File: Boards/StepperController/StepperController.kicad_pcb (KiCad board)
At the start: 2 copper layers, 164 parts, among them IC1 ATMEGA645A-A, J1 I2C, J2 SPI_Extern, J3 ISP, J4 Reference, J5 Display, J7 Spindle, P1 Power, P10 CONN_Z, P2 Cover, P3 USB_B, P4 Relay2, P5 Relay1, P6 Emer_Off, P8 CONN_X, P9 CONN_Y, Q1 BC817-40, Q2 BC817-40, Q3 BC817-40, Q4 BC817-40, Q5 BC817-40, SW2 SW_1, SW3 SW_2, U1 LM2595S-5, U2 74LS11, U3 FT232RL, U5 TMC2660, U6 TMC2660, U7 TMC2660, U8 74HC00, X1 16MHz, Y1 20MHz

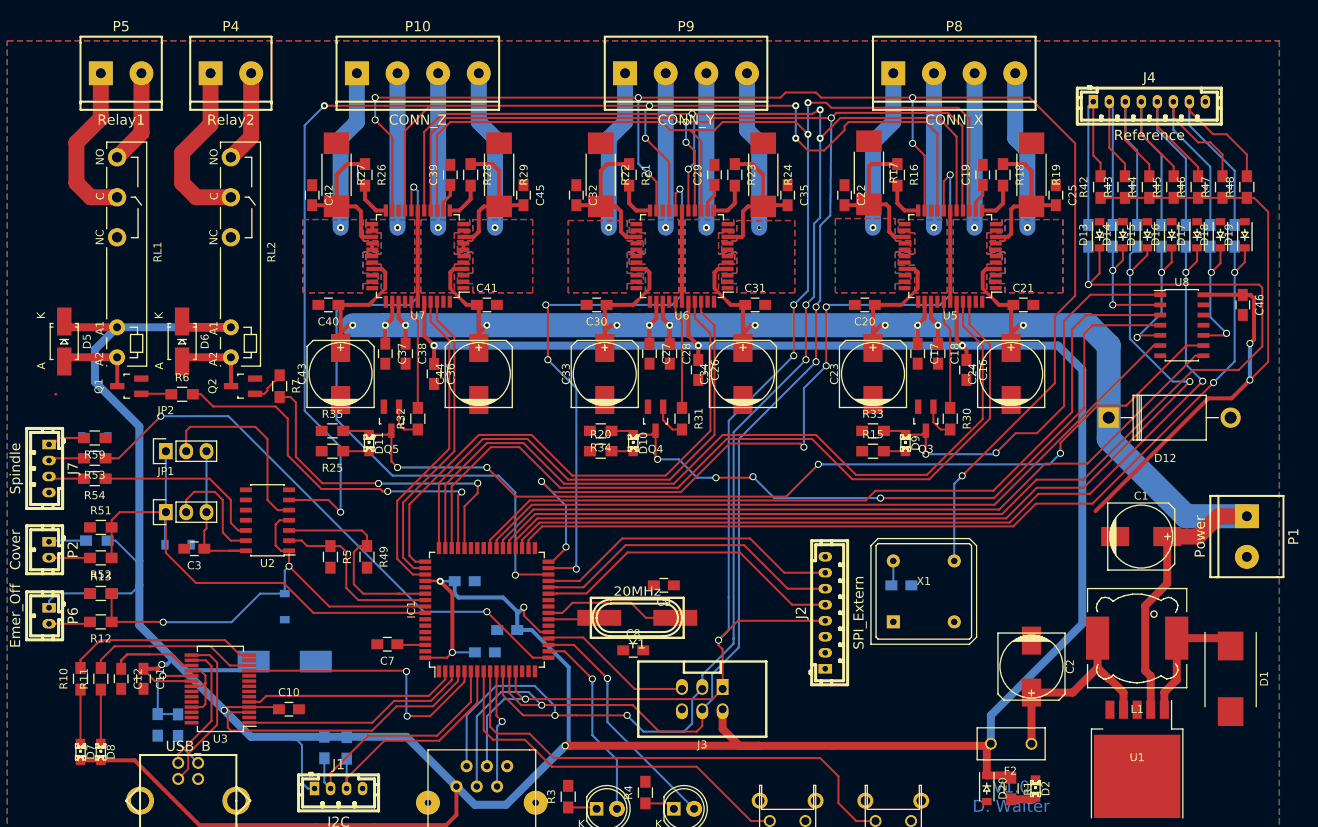
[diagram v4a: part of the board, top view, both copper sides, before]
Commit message: Layouting... Neuer Oszillator für TMC
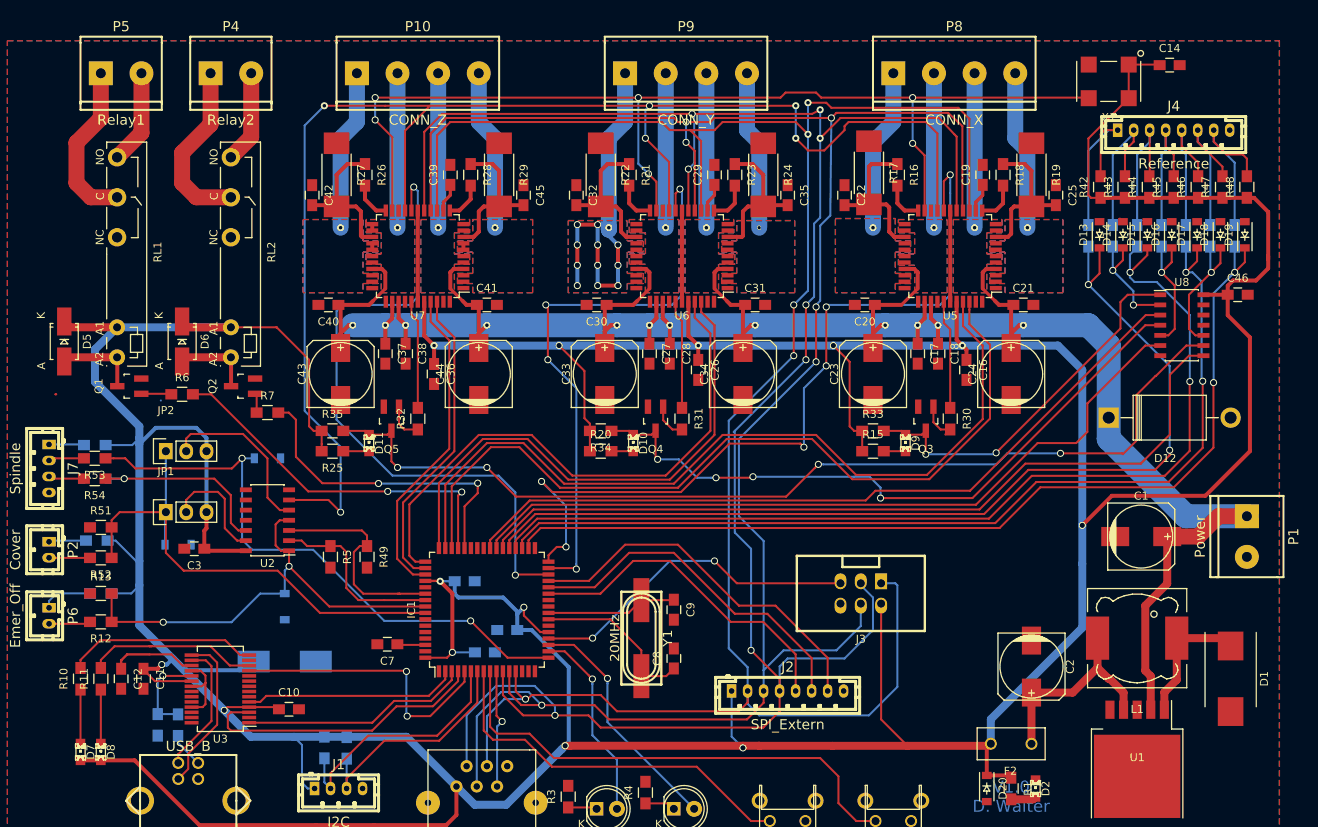
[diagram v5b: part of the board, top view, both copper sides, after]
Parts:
- C14: moved to F.Cu
- R59: moved to B.Cu
- X1: footprint Oscillators:OSC_DIP8 -> Oscillators_SMD:XO91
- moved C14 73.2 mm to (209.3, 56.9)
- moved X1 67.8 mm to (201.7, 58.9), turned to 180 degrees
- moved J3 23.8 mm to (170.7, 122.9)
- moved D22 21.8 mm to (96.5, 106.0), turned to 0 degrees
- moved J2 10.8 mm to (161.5, 135.1), turned to 0 degrees
- moved C8 5.18 mm to (147.3, 131.1), turned to 90 degrees
- moved J4 4.68 mm to (209.8, 65.0)
- moved R7 3.64 mm to (96.5, 100.3), turned to 0 degrees
- moved C9 3.29 mm to (147.3, 125.0), turned to 270 degrees
- moved Y1 2.59 mm to (143.3, 128.5), turned to 270 degrees
- moved C46 1.42 mm to (217.8, 85.6), turned to 0 degrees
- moved R59 0.89 mm to (74.9, 104.4)
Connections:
- J2 pad 2: /Controller/SCK -> /Controller/SDO
- J2 pad 4: /Controller/SDO -> /Controller/SCK
- X1 pad 1: (no net) -> +5V
- X1 pad 4: GND -> +5V
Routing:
- net +5V: track 625.9 -> 734.7 mm, vias 11 -> 13
- net /Driver/Driver_X/TMC_Clock: track 193.6 -> 134.5 mm, vias 7 -> 6
- net /Controller/SCK: track 235.0 -> 267.6 mm
- net /Controller/SDO: track 236.2 -> 265.0 mm, vias 6 -> 5
- net /Driver/Driver_Y/OB1_Y: track 20.1 -> 48.7 mm, vias 1 -> 12
- net Net-(IC1-Pad20): track 19.4 -> 41.8 mm, vias 0 -> 2
- net /Controller/SDI: track 231.2 -> 252.5 mm
- net /Controller/Ref_X1: track 144.3 -> 123.4 mm, vias 1 -> 2
- net Net-(C8-Pad1): track 6.42 -> 20.9 mm
- net Net-(J4-Pad6): track 30.1 -> 19.6 mm
- net Net-(J4-Pad5): track 28.3 -> 18.7 mm
- net Net-(J4-Pad7): track 31.0 -> 21.6 mm
- net Net-(J4-Pad4): track 28.2 -> 19.0 mm
- net Net-(J4-Pad3): track 27.4 -> 19.1 mm
- net Net-(IC1-Pad29): track 38.6 -> 46.8 mm
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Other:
- rule trace_min: 0.15 -> 0.254

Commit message: Layouting...
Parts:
- added G***: LOGO, Loewe:Loewe_Klein, F.Cu at (178.8, 139.2)
- added REF**: EuroBoard160mmX100mm_holes, Euro:EuroBoard160mmX100mm_holes, F.Cu at (64.0, 152.9)
- added REF**: Symbol_HighVoltage_Type2_CopperTop_VerySmall, Symbols:Symbol_HighVoltage_Type2_CopperTop_VerySmall, B.Cu at (84.8, 79.2)
- C11: moved to B.Cu
- moved C11 3.82 mm to (77.2, 133.9), turned to 180 degrees
- moved X1 2.80 mm to (204.5, 59.1)
- moved D2 2.74 mm to (189.9, 148.0), turned to 0 degrees
- moved J7 2.62 mm to (69.8, 104.8)
- moved D20 2.29 mm to (184.2, 147.3)
- moved C14 2.16 mm to (210.8, 58.4), turned to 90 degrees
- moved P2 1.42 mm to (69.8, 116.2)
- moved P6 1.42 mm to (69.8, 127.0)
- moved R1 1.33 mm to (189.9, 146.1), turned to 0 degrees
- moved C17 1.02 mm to (176.8, 93.0)
- moved C28 1.02 mm to (145.8, 93.0)
- moved C34 1.02 mm to (157.0, 95.5)
- moved P8 1.02 mm to (181.4, 57.9)
- moved C43 1.02 mm to (104.6, 95.5)
- moved C18 1.02 mm to (179.3, 93.0)
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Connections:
- net /Driver/Driver_Y/BRN_Y renamed /Driver/Driver_Y/BRB_Y
- R28 pad 2: /Driver/Driver_Z/BRB_Z -> /Driver/Driver_Z/SRA_Z
- U7 pad 12: /Driver/Driver_Z/BRB_Z -> /Driver/Driver_Z/SRA_Z
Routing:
- net GND: track 43.6 -> 207.2 mm, vias 0 -> 16
- net /Driver/Driver_Z/OB1_Z: track 20.9 -> 53.1 mm, vias 1 -> 12
- net /Driver/Driver_Y/OA1_Y: track 19.9 -> 51.1 mm, vias 1 -> 11
- net /Driver/Driver_X/OA1_X: track 19.9 -> 50.2 mm, vias 1 -> 12
- net /Driver/Driver_X/OB1_X: track 20.4 -> 49.9 mm, vias 1 -> 12
- net /Driver/Driver_Z/OA1_Z: track 20.9 -> 47.9 mm, vias 1 -> 11
- net /Driver/Sup_36V: track 309.7 -> 295.4 mm
- net +5V: track 734.7 -> 748.2 mm
- net /Driver/Driver_Y/OB2_Y: track 19.3 -> 27.0 mm, vias 1 -> 5
- net /Driver/Driver_X/TMC_Enable: track 183.0 -> 190.4 mm
- net /Driver/Driver_Y/OA2_Y: track 19.3 -> 26.6 mm, vias 1 -> 4
- net /Driver/Driver_Z/OB2_Z: track 20.1 -> 27.2 mm, vias 1 -> 4
- net /Driver/Driver_Z/OA2_Z: track 19.3 -> 26.4 mm, vias 1 -> 4
- net /Driver/Driver_X/OA2_X: track 19.3 -> 26.1 mm, vias 1 -> 4
- net /Driver/Driver_X/OB2_X: track 19.3 -> 26.0 mm, vias 1 -> 4
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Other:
- board outline added: 160 x 100 mm
- board text added: "Bot"
- board text added: "TMC226 StepperController"
- board text added: "Top"

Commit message: Minor layout changes
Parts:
- moved G*** 3.34 mm to (179.3, 135.9)
- moved D3 1.52 mm to (137.7, 148.3)
- moved D4 1.52 mm to (147.3, 148.3)
- moved SW2 0.38 mm to (161.5, 150.0)
- moved SW3 0.38 mm to (174.8, 150.0)
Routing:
- net Net-(D3-Pad2): track 24.4 -> 22.9 mm
- net Net-(D3-Pad1): track 3.63 -> 4.76 mm
- net Net-(D4-Pad2): track 29.9 -> 30.8 mm
- net Net-(P4-Pad1): track 18.6 -> 19.5 mm
- net Net-(P5-Pad1): track 18.5 -> 19.1 mm

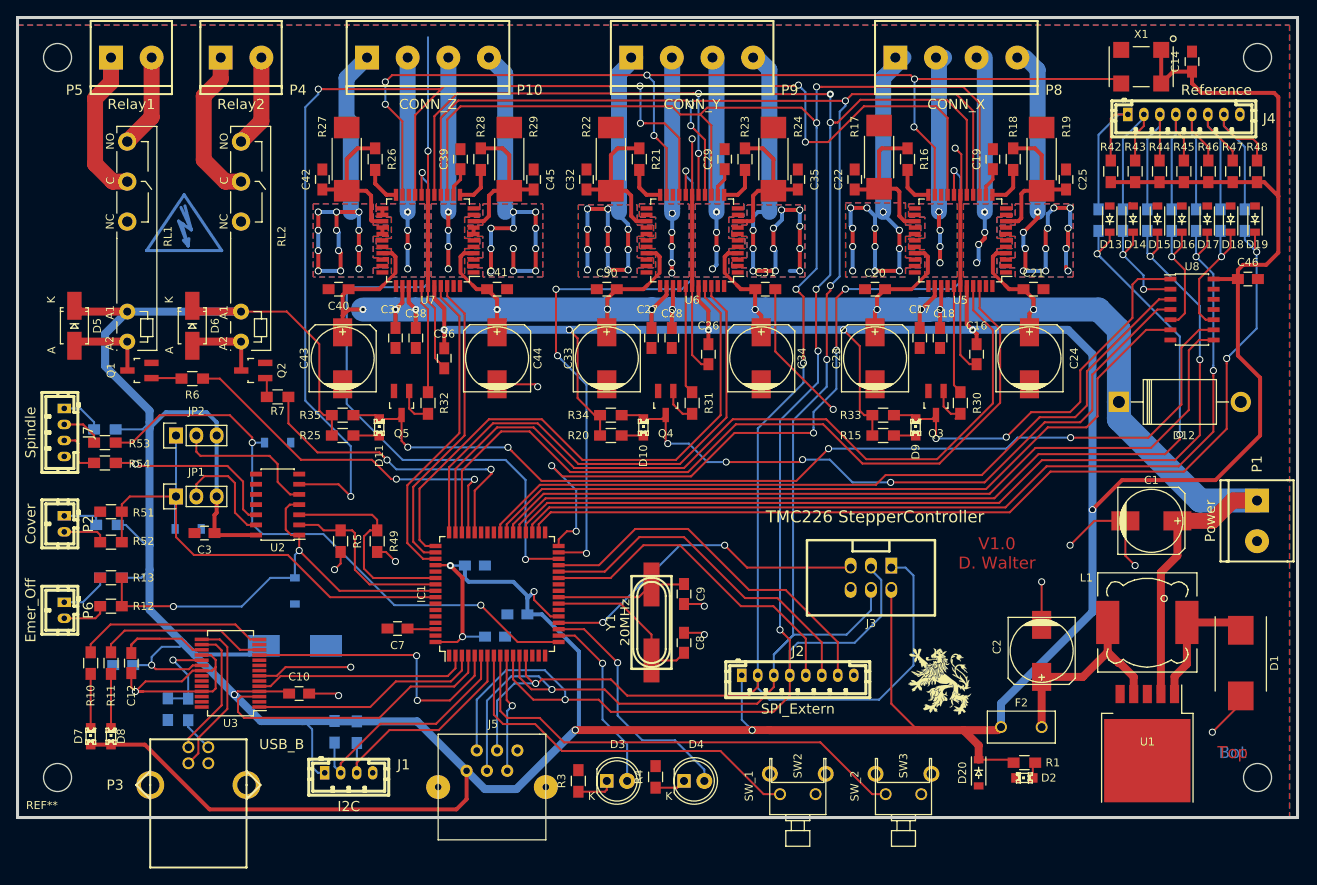
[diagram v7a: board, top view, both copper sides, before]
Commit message: Fixed Part Libraries
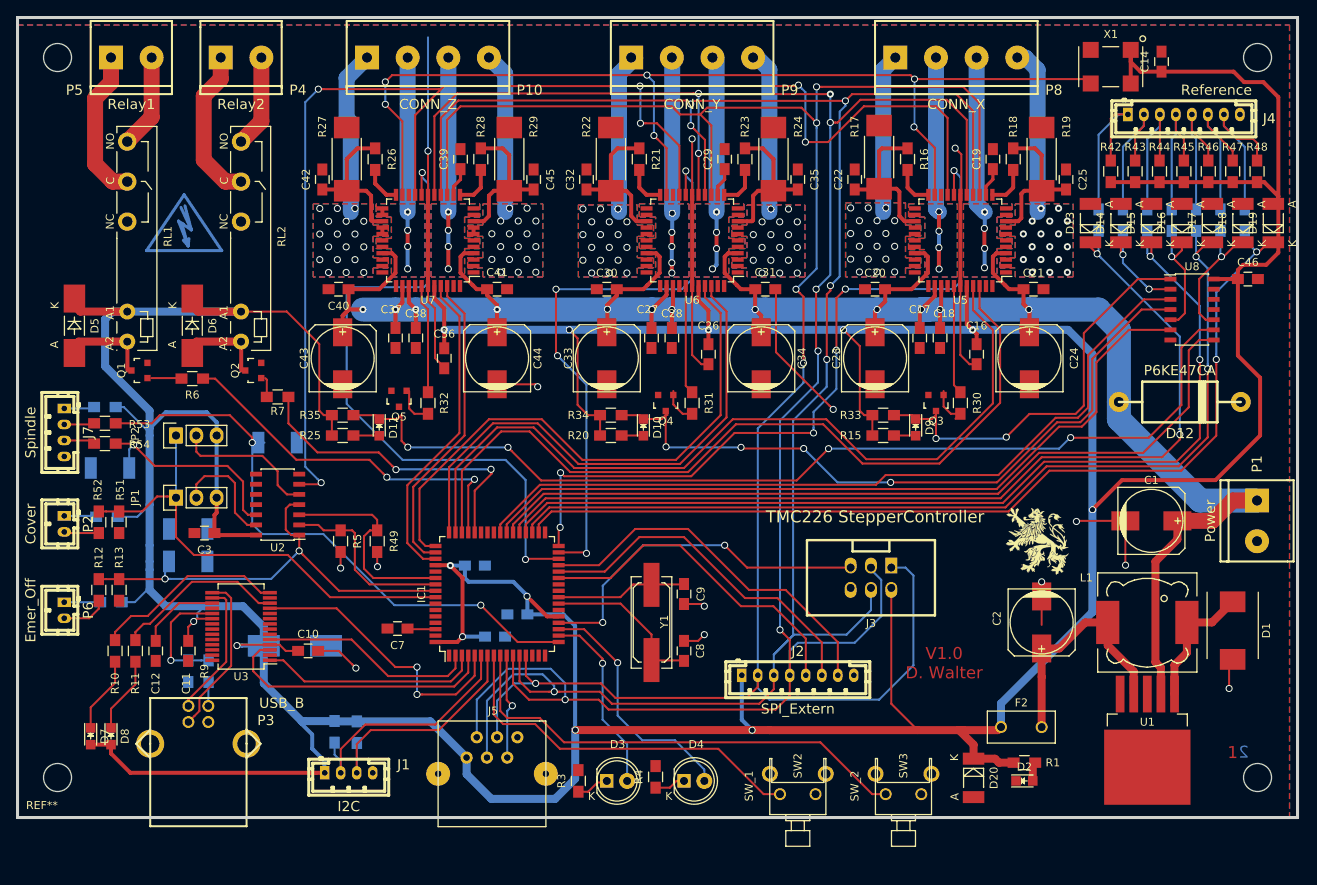
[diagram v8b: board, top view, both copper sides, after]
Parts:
- C11: moved to F.Cu
- D1: footprint Diodes_SMD:Diode-DO-214AB_Handsoldering -> Diodes_SMD:DO-214AB
- D10, D11, D2, D7, D8, D9: footprint LEDs:LED-0805 -> LEDs:LED_0805
- D12: footprint Diodes_ThroughHole:Diode_DO-201AD_Horizontal_RM15 -> w_pth_diodes:diode_do201
- D13, D14, D16, D17, D18, D19, D21, D22, D23, D29: value 5V -> ZMY5,6; footprint Diodes_SMD:SOD-123 -> Diodes_SMD:MELF_Standard
- D15, D20: footprint Diodes_SMD:SOD-123 -> Diodes_SMD:MELF_Standard
- D5, D6: footprint Diodes_SMD:Diode-SMA_Handsoldering -> Diodes_SMD:MELF_Handsoldering
- JP1, JP2: footprint Socket_Strips:Socket_Strip_Straight_1x03 -> Pin_Headers:Pin_Header_Straight_1x03
- Q1, Q2, Q3, Q4, Q5: footprint Housings_SOT-23_SOT-143_TSOT-6:SOT-23_Handsoldering -> TO_SOT_Packages_SMD:SOT-23
- U1: footprint SMD_Packages:TO-263-5_HandSoldering -> TO_SOT_Packages_SMD:TO-263-5Lead
- Y1: footprint w_crystal:hc-49_smd -> Crystals:Q_49U3HMS
- moved G*** 21.3 mm to (191.5, 118.4)
- moved D21 13.8 mm to (85.3, 120.9), turned to 0 degrees
- moved C11 8.32 mm to (85.3, 132.1), turned to 270 degrees
- moved D12 7.62 mm to (209.3, 101.0)
- moved U3 5.98 mm to (91.9, 129.0)
- moved C10 5.45 mm to (100.3, 132.1)
- moved R8 5.41 mm to (87.9, 134.6)
- moved R9 5.38 mm to (85.3, 134.6)
- moved P3 5.16 mm to (86.6, 146.0)
- moved D1 4.19 mm to (215.9, 129.5)
- moved C14 3.81 mm to (207.0, 58.4)
- moved X1 3.81 mm to (200.7, 59.1)
- moved C2 3.56 mm to (192.0, 128.5)
- moved C12 3.41 mm to (81.3, 132.1)
- moved R10 3.41 mm to (76.2, 132.1)
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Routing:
- net /Controller/Stall_Z: track 125.2 -> 15.7 mm, vias 4 -> 0
- net GND: track 207.2 -> 270.5 mm, vias 16 -> 18
- net /Driver/Driver_Z/OB1_Z: track 53.1 -> 21.4 mm, vias 12 -> 1
- net /Driver/Driver_Y/OA1_Y: track 51.1 -> 19.9 mm, vias 11 -> 1
- net /Driver/Driver_X/OB1_X: track 49.9 -> 20.2 mm, vias 12 -> 1
- net /Driver/Driver_X/OA1_X: track 50.2 -> 21.0 mm, vias 12 -> 1
- net /Driver/Driver_Y/OB1_Y: track 49.7 -> 20.6 mm, vias 11 -> 1
- net /Driver/Driver_Z/OA1_Z: track 47.9 -> 21.0 mm, vias 11 -> 1
- net +5V: track 748.2 -> 737.8 mm
- net /Driver/Driver_X/TMC_Enable: track 190.4 -> 182.4 mm
- net /Controller/CS_X: track 100.1 -> 95.0 mm
- net /Controller/Cover: track 64.3 -> 60.2 mm
- net /Driver/Driver_X/TMC_Clock: track 139.3 -> 135.5 mm
- net Net-(C2-Pad1): track 26.3 -> 29.9 mm
- net Net-(R8-Pad2): track 11.8 -> 15.1 mm
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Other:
- board text added: "1"
- board text added: "2"
- board text removed: "Bot"
- board text removed: "Top"
